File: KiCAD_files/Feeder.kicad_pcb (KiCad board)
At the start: 2 copper layers, 37.3 x 55.2 mm, 58 parts, among them J1 Conn_01x01, J2 Conn_01x01, J3 Conn_01x01, J4 Conn_01x01, Q1 TK13P25D,RQ, T1 PA2467NL, U2 NCP12700, U3 HMHA2801A, U4 TL431MFDT,215

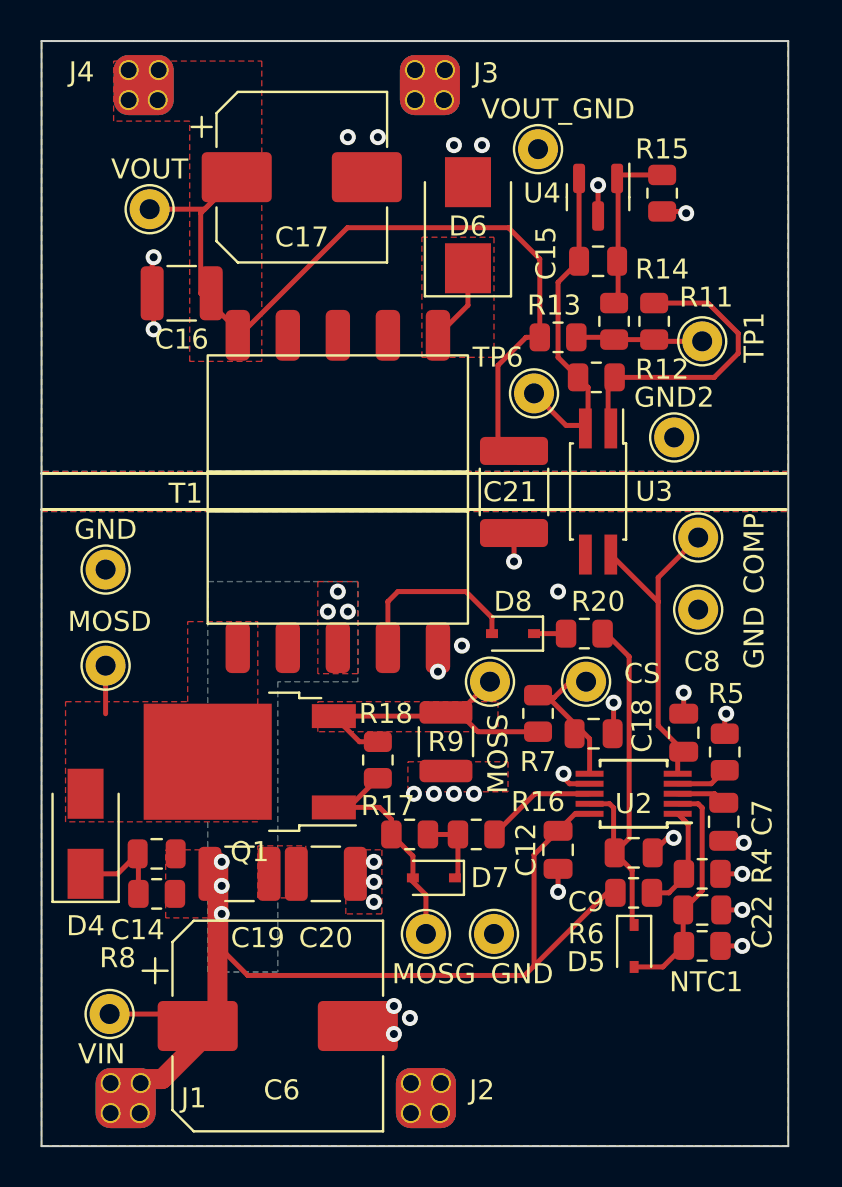
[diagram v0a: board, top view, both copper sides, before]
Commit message: Created a first routed STM32G4 module and ordered it in JLCPCB
Former-commit-id: 49804de64bb80eadc7f05c9bfca13c93680f06aa
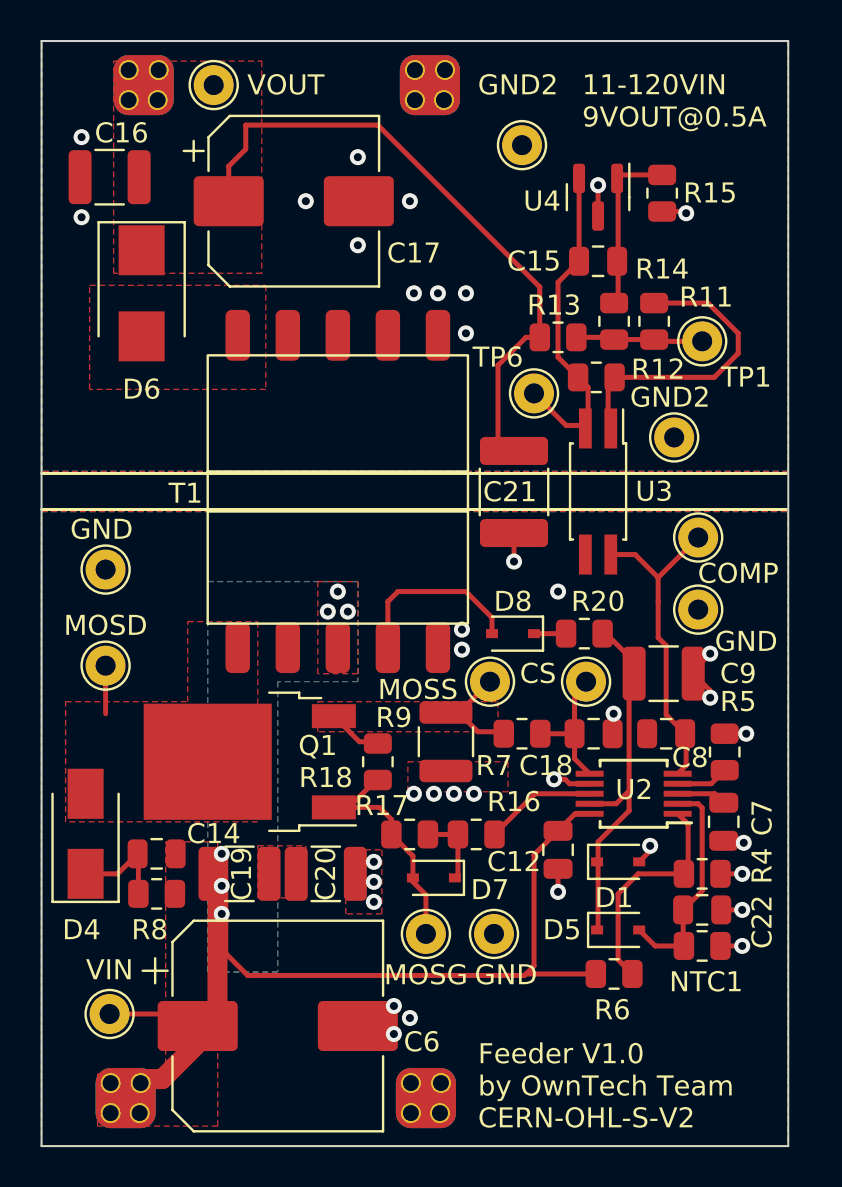
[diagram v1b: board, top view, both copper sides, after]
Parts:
- added D1: 9.1V, Diode_SMD:D_SOD-323, F.Cu at (77.0, 62.0)
- C12: value 100nF -> X7T, 100nF
- C18: value 100pF -> C0G, 100pF
- C21: value 1nF -> 680pF
- C6: value 100uF -> 3.3uF, 400V
- C9: value 2.2uF -> 10uF; footprint Capacitor_SMD:C_0805_2012Metric -> Capacitor_SMD:C_1210_3225Metric
- COMP1: renamed from COMP; value TestPoint -> COMP
- CS1: renamed from CS; value TestPoint -> CS
- GND1, GND3, GND4: renamed from GND; value TestPoint -> GND
- GND2: value TestPoint -> GND2
- MOSD1: renamed from MOSD; value TestPoint -> MOSD
- MOSG1: renamed from MOSG; value TestPoint -> MOSG
- MOSS1: renamed from MOSS; value TestPoint -> MOSS
- R15: value 10k -> 14.7k
- R4: value 12.4k -> 27k
- R6: value 158k -> 348K
- R7: value 500 -> 470
- VIN1: renamed from VIN; value TestPoint -> VIN
- VOUT1: renamed from VOUT; value TestPoint -> VOUT
- VOUT_GND1: renamed from VOUT_GND; value TestPoint -> GND2
- moved D6 16.7 mm to (53.2, 33.6), turned to -90 degrees
- moved C9 9.07 mm to (79.3, 52.6)
- moved VOUT1 6.98 mm to (56.8, 23.2)
- moved C16 6.83 mm to (51.6, 27.8)
- moved R6 4.17 mm to (76.8, 67.6)
- moved R7 1.29 mm to (72.2, 55.6), turned to 180 degrees
- moved C17 1.26 mm to (60.8, 29.0)
- moved D5 1.13 mm to (77.0, 65.4), turned to 0 degrees
- moved C8 0.88 mm to (79.4, 55.6), turned to 180 degrees
- moved VOUT_GND1 0.82 mm to (72.2, 26.2)
- moved R18 0.09 mm to (65.0, 57.0)
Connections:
- D6 pad 1: Net-(D6-Pad1) -> VOUT
- D6 pad 2: GND2 -> Net-(D6-Pad2)
- T1 pad 10: Net-(D6-Pad1) -> GND2
- T1 pad 6: VOUT -> Net-(D6-Pad2)
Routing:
- net VOUT: track 45.4 -> 31.2 mm
- net MOSS: track 15.5 -> 8.71 mm
- net Net-(R4-Pad1): track 5.72 -> 11.5 mm
- net Net-(D6-Pad1): track 3.97 -> 0.00 mm
- net GND2: track 5.43 -> 2.77 mm, vias 8 -> 12
- net Net-(C18-Pad1): track 8.01 -> 6.05 mm
- net VIN: track 57.2 -> 55.8 mm
- net VAUX: track 19.1 -> 18.4 mm
- net GND: track 14.9 -> 14.8 mm, vias 24 -> 25
- added copper zone on F.Cu, net Net-(D6-Pad2)
- removed copper zone on F.Cu, net Net-(D6-Pad1)
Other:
- board text added: "11-120VIN 9VOUT@0.5A"
- board text added: "CERN-OHL-S-V2"
- board text added: "Feeder V1.0 by OwnTech Team"

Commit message: [Feeder] WIP on the V2 redesign
Former-commit-id: 5bce92fb9a428cd005e74b891f189b6460f88472
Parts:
- removed COMP1: COMP, TestPoint:TestPoint_THTPad_D2.0mm_Drill1.0mm
- removed CS1: CS, TestPoint:TestPoint_THTPad_D2.0mm_Drill1.0mm
- removed MOSD1: MOSD, TestPoint:TestPoint_THTPad_D2.0mm_Drill1.0mm
- removed MOSG1: MOSG, TestPoint:TestPoint_THTPad_D2.0mm_Drill1.0mm
- removed MOSS1: MOSS, TestPoint:TestPoint_THTPad_D2.0mm_Drill1.0mm
- removed TP1, TP6: TestPoint, TestPoint:TestPoint_THTPad_D2.0mm_Drill1.0mm
- added C1: 1uF, Capacitor_SMD:C_0805_2012Metric, F.Cu at (78.0, 50.0)
- added C10: 10uF, Capacitor_SMD:C_1210_3225Metric, F.Cu at (76.8, 32.6)
- added C13: 10uF, Capacitor_SMD:C_1210_3225Metric, F.Cu at (113.0, 25.9)
- added C2: 100pF 1kV DNP, Capacitor_SMD:C_1206_3216Metric, F.Cu at (62.2, 54.0)
- added C3: 2.2nF, Capacitor_SMD:C_1812_4532Metric, F.Cu at (54.5, 43.4)
- added C4: 1nF 500V DNP, Capacitor_SMD:C_0805_2012Metric, F.Cu at (52.2, 38.6)
- added C5: 10uF, Capacitor_SMD:C_1210_3225Metric, F.Cu at (71.9, 32.6)
- added D2: BAS20HT1G, Diode_SMD:D_SOD-323, F.Cu at (75.8, 48.5)
- added J5: Conn_01x01, Footprints:Pad_terminal, F.Cu at (108.0, 34.0)
- added L1: 100uH, Inductor_SMD:L_0805_2012Metric, F.Cu at (75.8, 54.6)
- added Q2: 60V N channel, Package_TO_SOT_SMD:SOT-23, F.Cu at (73.0, 52.5)
- added R1: 1.4K, Resistor_SMD:R_0805_2012Metric, F.Cu at (71.6, 62.5)
- added R10: 10R 1W DNP, Resistor_SMD:R_2010_5025Metric, F.Cu at (50.4, 34.5)
- added R2: 1.4K, Resistor_SMD:R_0805_2012Metric, F.Cu at (73.5, 49.2)
- added U1: AP1117-50, Package_TO_SOT_SMD:SOT-223-3_TabPin2, F.Cu at (70.6, 26.5)
- added U5: AP1117-33, Package_TO_SOT_SMD:SOT-223-3_TabPin2, F.Cu at (77.9, 26.5)
- C21: value 680pF -> 2.2nF
- C9: value 10uF -> 1uF; footprint Capacitor_SMD:C_1210_3225Metric -> Capacitor_SMD:C_0805_2012Metric
- D1: value 9.1V -> BAS20HT1G
- D5: value 9.1V -> 6.2V
- R15: value 14.7k -> 27k
- moved J4 76.1 mm to (117.1, 64.7)
- moved J3 65.9 mm to (122.0, 60.5)
- moved C21 21.3 mm to (50.5, 43.4)
- moved D5 12.4 mm to (78.0, 53.0), turned to -90 degrees
- moved U4 12.2 mm to (79.3, 40.5), turned to 0 degrees
- moved NTC1 11.1 mm to (79.5, 55.2)
- moved GND2 9.48 mm to (89.0, 38.5)
- moved C15 9.27 mm to (75.5, 41.2), turned to 180 degrees
- moved R15 9.15 mm to (79.0, 37.8), turned to 0 degrees
- moved VOUT_GND1 8.98 mm to (71.5, 17.2)
- moved C22 8.07 mm to (73.3, 62.5), turned to 90 degrees
- moved C9 8.06 mm to (71.8, 55.5), turned to 90 degrees
- moved D1 7.46 mm to (73.8, 55.2), turned to 90 degrees
- moved C18 6.65 mm to (69.2, 56.4), turned to 180 degrees
- moved R4 6.10 mm to (75.1, 62.5), turned to -90 degrees
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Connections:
- C9 pad 1: VAUX -> VBoost
- D1 pad 1: VAUX -> VBoost
- D1 pad 2: GND -> Net-(D1-Pad2)
- J3 pad 1: GND2 -> Net-(C10-Pad1)
- J4 pad 1: VOUT -> Net-(C10-Pad2)
- R20 pad 2: Net-(D8-Pad1) -> Net-(D2-Pad1)
- U2 pad 9: VAUX -> VBoost
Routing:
- net VOUT: track 31.2 -> 0.00 mm
- net VAUX: track 18.4 -> 4.66 mm
- net Net-(R11-Pad2): track 15.2 -> 4.73 mm
- net VBoost: track 0.00 -> 10.1 mm
- net Net-(R4-Pad1): track 11.5 -> 4.30 mm
- net Net-(D7-Pad2): track 12.4 -> 6.11 mm
- net Net-(C15-Pad1): track 16.9 -> 11.4 mm
- net GND: track 14.8 -> 9.91 mm, vias 25 -> 20
- net Net-(D2-Pad2): track 9.05 -> 13.5 mm
- net MOSS: track 8.71 -> 4.92 mm
- net Net-(C8-Pad1): track 16.2 -> 19.7 mm
- net Net-(D1-Pad2): track 0.00 -> 3.41 mm
- net Net-(R16-Pad1): track 5.59 -> 2.50 mm
- net Net-(R11-Pad1): track 6.37 -> 3.42 mm
- net VIN: track 55.8 -> 53.4 mm
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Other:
- board size 37.3 x 55.2 mm -> 34 x 55.2 mm

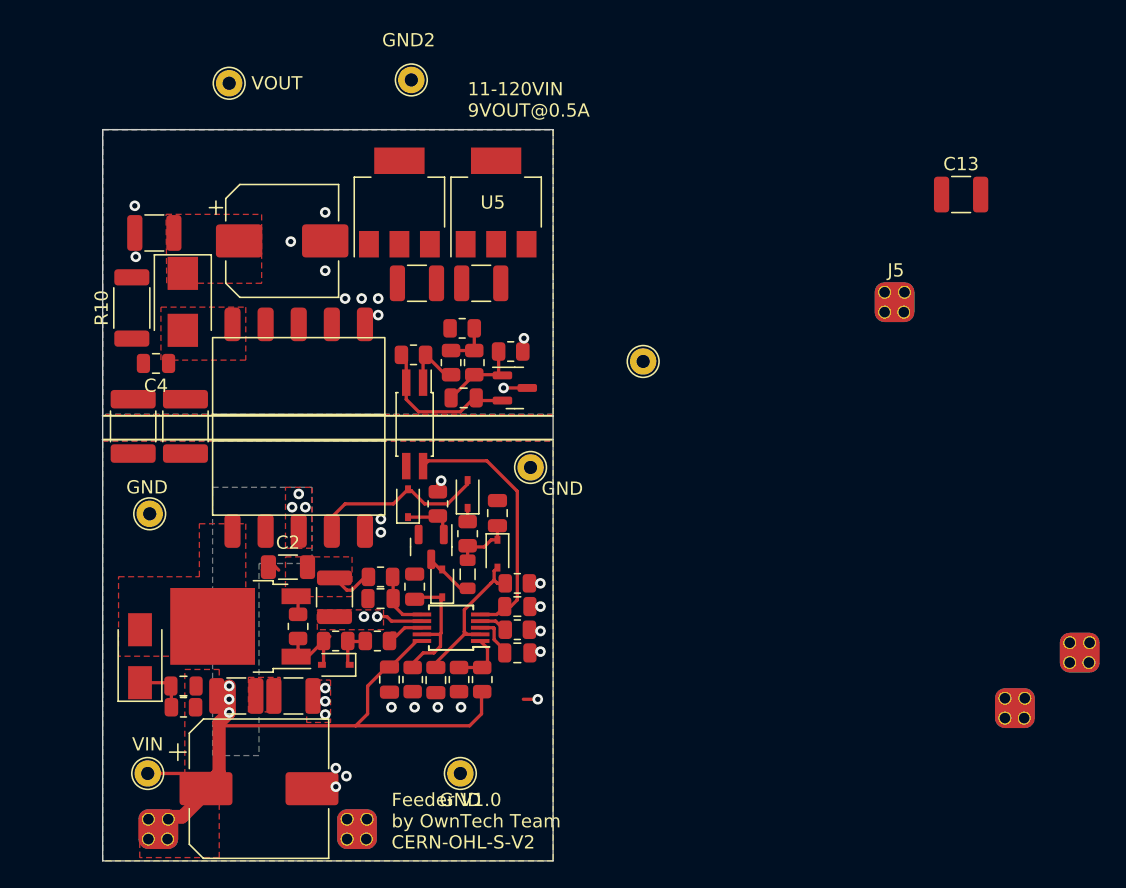
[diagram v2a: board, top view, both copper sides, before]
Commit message: WIP: mooving to a single board implementation with 160x100 form factor.
Former-commit-id: e8c19d5fc5237412fb5a003591d44756dbc6e173
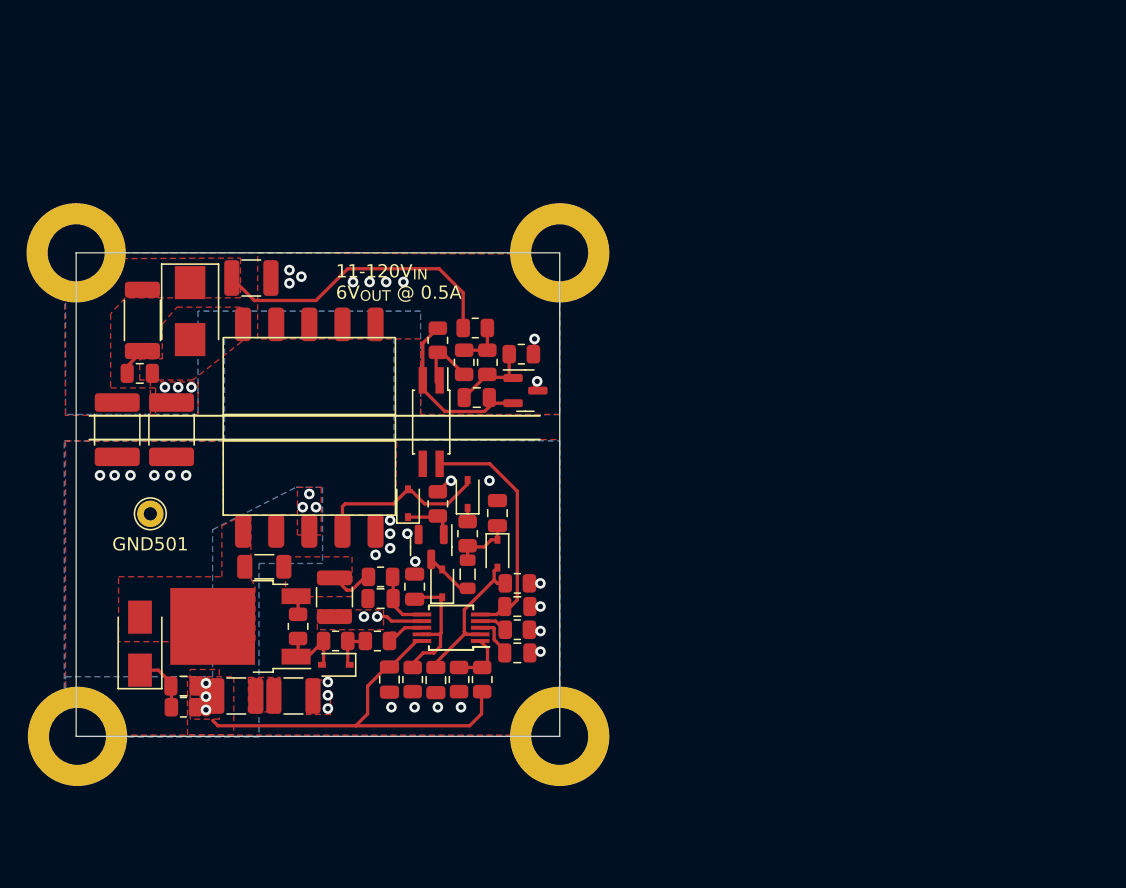
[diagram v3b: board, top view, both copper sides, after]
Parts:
- removed C10, C13, C5: 10uF, Capacitor_SMD:C_1210_3225Metric
- removed C17: 100uF, 35V, Capacitor_SMD:CP_Elec_8x10
- removed C6: 3.3uF, 400V, Capacitor_SMD:CP_Elec_10x10
- removed GND1, GND3, GND4: GND, TestPoint:TestPoint_THTPad_D2.0mm_Drill1.0mm
- removed GND2, VOUT_GND1: GND2, TestPoint:TestPoint_THTPad_D2.0mm_Drill1.0mm
- removed J1, J2, J3, J4, J5: Conn_01x01, Footprints:Pad_terminal
- removed U1: AP1117-50, Package_TO_SOT_SMD:SOT-223-3_TabPin2
- removed U5: AP1117-33, Package_TO_SOT_SMD:SOT-223-3_TabPin2
- removed VIN1: VIN, TestPoint:TestPoint_THTPad_D2.0mm_Drill1.0mm
- removed VOUT1: VOUT, TestPoint:TestPoint_THTPad_D2.0mm_Drill1.0mm
- added GND501: GND, TestPoint:TestPoint_THTPad_D2.0mm_Drill1.0mm, F.Cu at (51.8, 50.0)
- added J501: Conn_01x01, MountingHole:MountingHole_4.3mm_M4_DIN965_Pad, F.Cu at (46.3, 66.8)
- added J502: Conn_01x01, MountingHole:MountingHole_4.3mm_M4_DIN965_Pad, F.Cu at (82.7, 66.8)
- added J503: Conn_01x01, MountingHole:MountingHole_4.3mm_M4_DIN965_Pad, F.Cu at (46.2, 30.3)
- added J504: Conn_01x01, MountingHole:MountingHole_4.3mm_M4_DIN965_Pad, F.Cu at (82.7, 30.3)
- moved C515 8.08 mm to (59.4, 32.2), turned to 0 degrees
- moved R515 2.14 mm to (73.5, 36.9), turned to 90 degrees
- moved C511 1.79 mm to (60.4, 54.0)
- moved C514 1.44 mm to (51.0, 39.4)
- moved U502 1.26 mm to (73.0, 43.1)
- moved R513 1.23 mm to (51.2, 35.4)
- moved C513 1.23 mm to (49.3, 43.6)
- moved C512 1.08 mm to (53.4, 43.6)
- moved C516 0.99 mm to (76.4, 41.2)
- moved R514 0.99 mm to (75.5, 38.6)
- moved R516 0.99 mm to (76.3, 36.0)
- moved R517 0.99 mm to (77.2, 38.6)
- moved D504 0.95 mm to (51.0, 59.8)
- moved D507 0.89 mm to (54.8, 34.7)
- moved R518 0.82 mm to (79.8, 38.0)
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- renumbered C19 to C501, C20 to C502, C22 to C503, C7 to C504, C8 to C505, C18 to C506, C9 to C507, C12 to C508, C1 to C509, C14 to C510, C2 to C511, C3 to C512, C21 to C513, C4 to C514, C16 to C515, C15 to C516, D5 to D501, D1 to D502, D7 to D503, D4 to D504, D2 to D505, D8 to D506, D6 to D507, L1 to L501, NTC1 to NTC501, Q2 to Q501, Q1 to Q502, R6 to R501, R4 to R502, R5 to R503, R1 to R504, R16 to R505, R7 to R506, R17 to R507, R18 to R508, R8 to R509, R9 to R510, R20 to R511, R2 to R512, R10 to R513, R11 to R514, R12 to R515, R13 to R516, R14 to R517, R15 to R518, T1 to T501, U2 to U501, U3 to U502, U4 to U503
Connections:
- net GND2 renamed DGND
- net VIN renamed /VIN
- net VOUT renamed /VOUT
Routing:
- net /VOUT: track 0.00 -> 23.9 mm
- net /VIN: track 53.4 -> 33.6 mm
- net Net-(C514-Pad2): track 0.00 -> 2.16 mm
- net Net-(C516-Pad1): track 11.4 -> 13.2 mm
- net Net-(C505-Pad1): track 19.7 -> 18.2 mm
- net MOSD: track 1.43 -> 0.00 mm
- net Net-(D505-Pad2): track 13.5 -> 12.3 mm
- net Net-(D503-Pad2): track 6.11 -> 5.12 mm
- net GND: track 9.91 -> 9.09 mm, vias 20 -> 27
- net DGND: track 2.57 -> 1.97 mm, vias 11 -> 12
- net Net-(C510-Pad2): track 4.53 -> 3.97 mm
- added copper zone on In1.Cu, net DGND
- added copper zone on In1.Cu, net GND
- added copper zone on In2.Cu, net GND
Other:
- board size 34 x 55.2 mm -> 36.5 x 36.5 mm
- copper layers 2 -> 4
- board text added: "11-120V_{IN} 6V_{OUT} @ 0.5A"
- board text added: "Feeder V1.1 by OwnTech Team"
- board text removed: "11-120VIN 9VOUT@0.5A"
- board text removed: "Feeder V1.0 by OwnTech Team"
